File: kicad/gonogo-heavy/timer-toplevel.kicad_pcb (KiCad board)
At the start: 2 copper layers, 234.9 x 79.9 mm, 94 parts, among them J1 Screw_Terminal_01x02, J2 Screw_Terminal_01x04, J3 Raspberry_Pi_2_3, K1 FINDER-30.22, Q1 2N2222, Q2 2N2222, SW1 SW_DIP_x08, SW2 SW_DIP_x04, SW3 SW_DIP_x08, SW4 SW_DIP_x04, T1 MountingHole_2.7mm_M2.5_DIN965, T2 MountingHole_2.7mm_M2.5_DIN965, T3 MountingHole_2.7mm_M2.5_DIN965, T4 MountingHole_2.7mm_M2.5_DIN965, T5 MountingHole_2.7mm_M2.5_DIN965, T6 MountingHole_2.7mm_M2.5_DIN965, T7 MountingHole_2.7mm_M2.5_DIN965, T8 MountingHole_2.7mm_M2.5_DIN965, T9 MountingHole_2.7mm_M2.5_DIN965, U1 4011, U10 4071, U11 4012, U12 4012, U13 4011, U14 4071, U15 4040, U16 4068, U17 4071, U18 4071, U19 4012, U2 4071, U20 MCP23017_SP, U21 MCP23017_SP, U3 4040, U4 4060, U5 4068, U6 4071, U7 4013, U8 4011, U9 4040, Y1 32,768 kHz

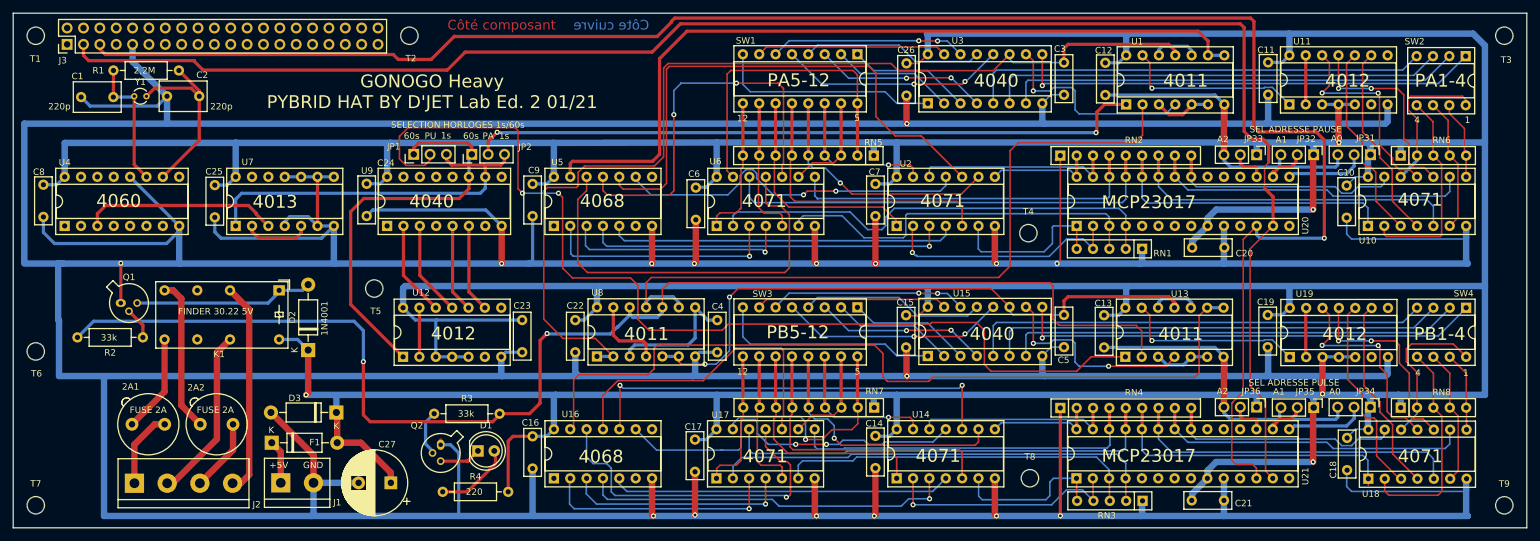
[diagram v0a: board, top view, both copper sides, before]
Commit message: Correction d'une erreur dans le schéma et le pcb
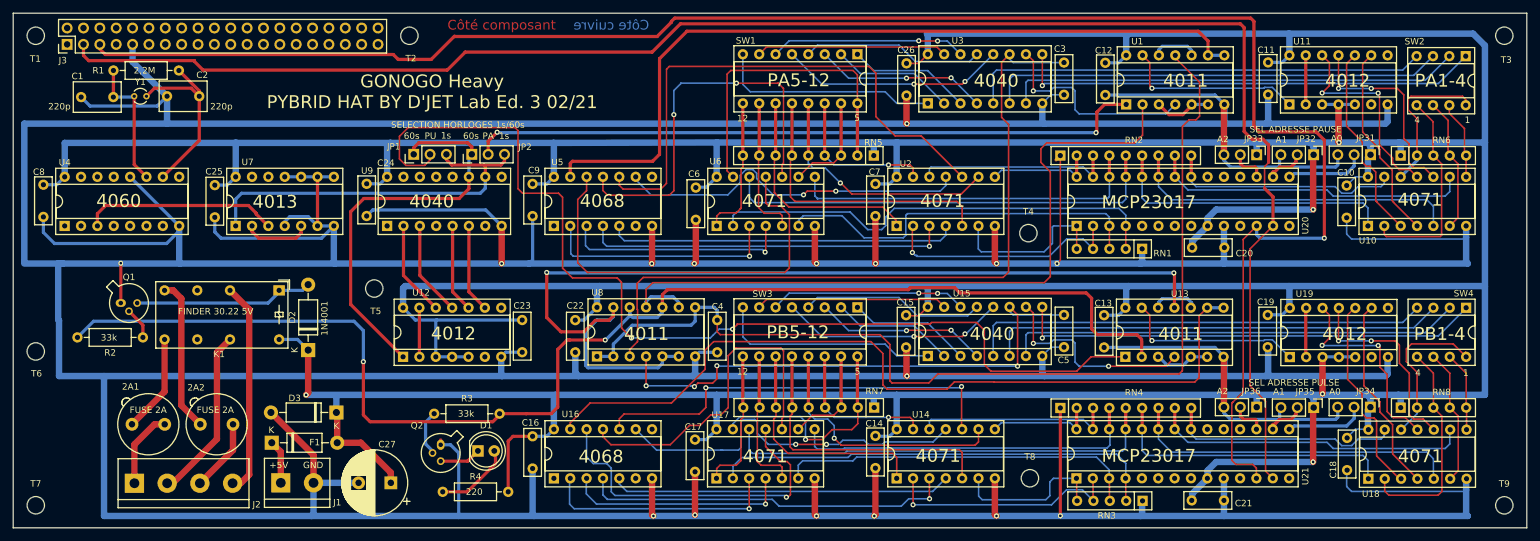
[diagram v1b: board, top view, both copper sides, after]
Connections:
- C4 pad 2: /Pulse-pause timer 1 de 2/&PPA1-12 -> /Pulse-pause timer 1 de 2/~&PPA1-12
- U1 pad 11: /Pulse-pause timer 1 de 2/RSTPA -> /Pulse-pause timer 1 de 2/~&PPA1-12
- U13 pad 11: /Pulse-pause timer 1 de 2/RSTPU -> /Pulse-pause timer 1 de 2/~&PUA1-12
- U8 pad 1: /Pulse-pause timer 1 de 2/RSTPA -> /Pulse-pause timer 1 de 2/~&PPA1-12
- U8 pad 13: /Pulse-pause timer 1 de 2/&PUA1-12 -> /Pulse-pause timer 1 de 2/~&PUA1-12
- U8 pad 2: /Pulse-pause timer 1 de 2/RSTPA -> /Pulse-pause timer 1 de 2/~&PPA1-12
- U8 pad 3: /Pulse-pause timer 1 de 2/&PPA1-12 -> /Pulse-pause timer 1 de 2/RSTPA
- U8 pad 4: /Pulse-pause timer 1 de 2/&PUA1-12 -> /Pulse-pause timer 1 de 2/RSTPU
- U8 pad 5: /Pulse-pause timer 1 de 2/RSTPU -> /Pulse-pause timer 1 de 2/~&PUA1-12
- U8 pad 6: /Pulse-pause timer 1 de 2/RSTPU -> /Pulse-pause timer 1 de 2/~&PUA1-12
- U8 pad 8: /Pulse-pause timer 1 de 2/&PPA1-12 -> /Pulse-pause timer 1 de 2/~&PPA1-12
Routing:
- net /Pulse-pause timer 1 de 2/~&PPA1-12: track 0.00 -> 159.6 mm
- net /Pulse-pause timer 1 de 2/~&PUA1-12: track 0.00 -> 151.4 mm, vias 0 -> 2
- net /Pulse-pause timer 1 de 2/RSTPA: track 157.9 -> 115.9 mm
- net /Pulse-pause timer 1 de 2/&PPA1-12: track 21.0 -> 0.00 mm
- net /Pulse-pause timer 1 de 2/RSTPU: track 96.8 -> 84.6 mm, vias 2 -> 4
- net /Pulse-pause timer 1 de 2/&PUA1-12: track 11.9 -> 0.00 mm
- net /Pulse-pause timer 1 de 2/PPU6: track 49.1 -> 53.4 mm
- net /Pulse-pause timer 1 de 2/PAUSE_ENABLE: track 113.1 -> 115.7 mm
- net /Pulse-pause timer 1 de 2/CLK-PULSE: track 158.7 -> 160.8 mm
- net /Pulse-pause timer 1 de 2/PPU8: track 67.2 -> 65.3 mm
- net Net-(U13-Pad8): track 127.3 -> 126.2 mm
- net /Pulse-pause timer 1 de 2/U4: track 46.1 -> 45.1 mm
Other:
- board text added: "GONOGO Heavy PYBRID HAT BY D'JET Lab Ed. 3 02/21"
- board text removed: "GONOGO Heavy PYBRID HAT BY D'JET Lab Ed. 2 01/21"

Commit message: décalage des condensateurs 100nF dans pcb
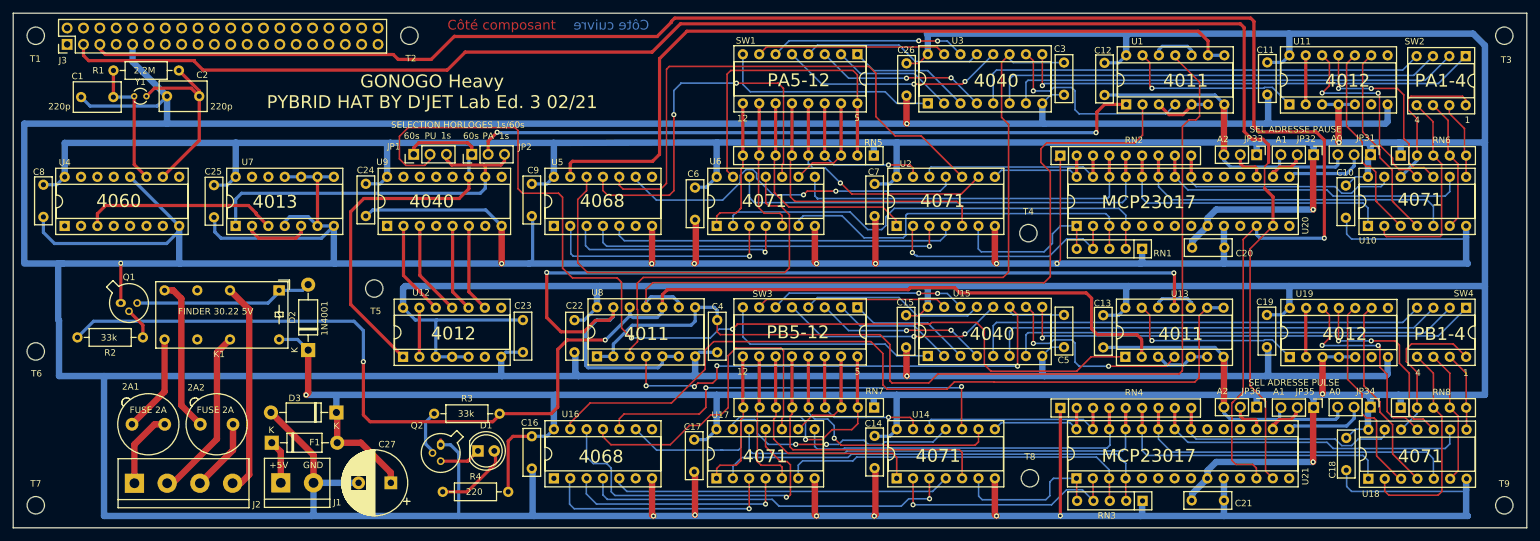
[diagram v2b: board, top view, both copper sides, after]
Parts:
- moved C10 0.12 mm to (243.2, 96.6)
- moved C11 0.12 mm to (231.0, 77.5)
- moved C12 0.12 mm to (205.8, 77.5)
- moved C13 0.12 mm to (205.6, 116.7)
- moved C14 0.12 mm to (170.1, 135.5)
- moved C16 0.12 mm to (116.9, 135.5)
- moved C17 0.12 mm to (142.1, 136.0)
- moved C18 0.12 mm to (243.3, 135.8)
- moved C19 0.12 mm to (231.0, 116.7)
- moved C22 0.12 mm to (123.5, 117.5)
- moved C23 0.12 mm to (115.5, 112.5)
- moved C24 0.12 mm to (91.1, 91.3)
- moved C25 0.12 mm to (67.5, 96.5)
- moved C6 0.12 mm to (142.2, 96.9)
- moved C7 0.12 mm to (170.1, 96.3)
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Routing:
- net /Pulse-pause timer 1 de 2/PPA7: track 56.0 -> 56.7 mm
- net /Pulse-pause timer 1 de 2/P9: track 25.8 -> 25.1 mm

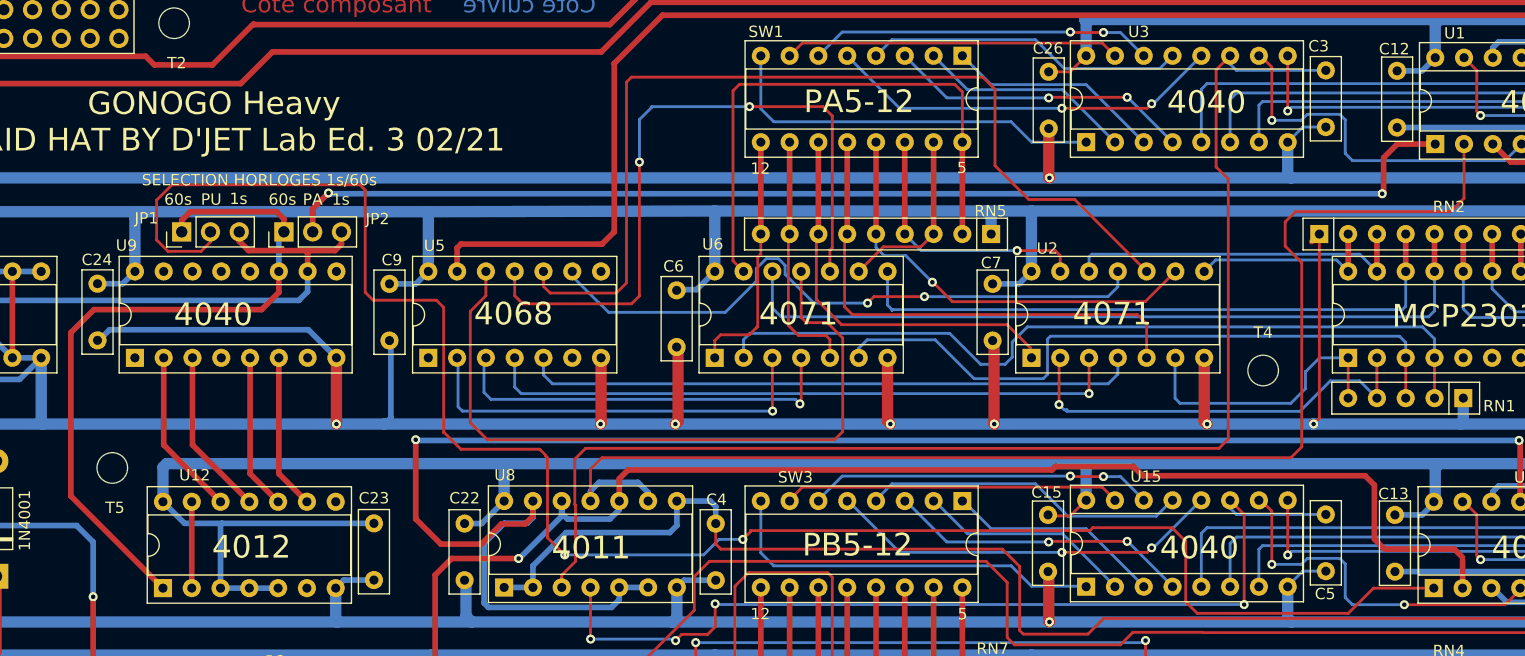
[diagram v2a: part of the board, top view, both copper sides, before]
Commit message: correction des erreurs et ajout de capas de reset sur poweron
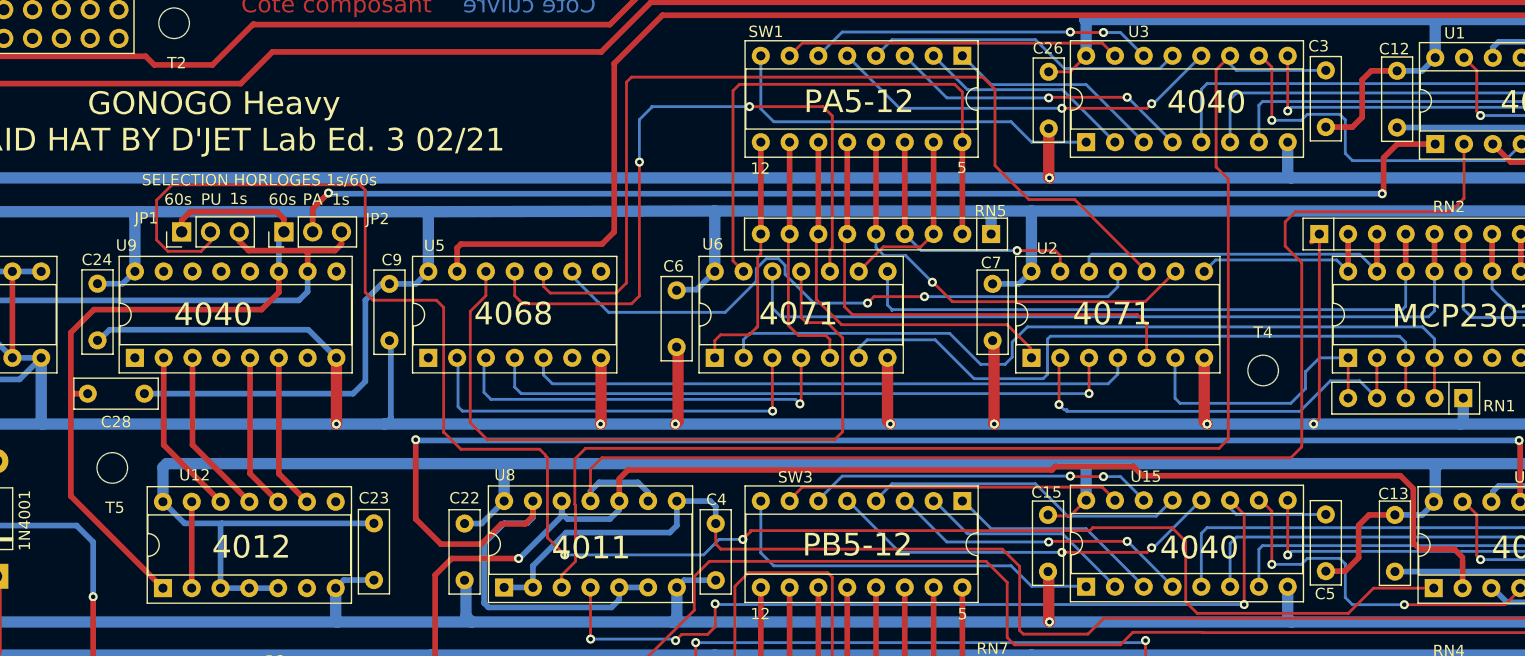
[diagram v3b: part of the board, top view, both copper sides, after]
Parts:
- added C28: 100nF, Capacitor_THT:C_Rect_L7.2mm_W2.5mm_P5.00mm_FKS2_FKP2_MKS2_MKP2, F.Cu at (95.2, 101.0)
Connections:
- C3 pad 1: GND -> VDD
- C5 pad 1: GND -> VDD
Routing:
- net VDD: track 1043.0 -> 1092.9 mm
- net GND: track 1458.9 -> 1451.0 mm
- net /Pulse-pause timer 1 de 2/60sec: track 63.0 -> 64.6 mm
